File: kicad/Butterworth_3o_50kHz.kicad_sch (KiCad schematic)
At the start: 31 parts, among them J1 Conn_01x02_Pin, J2 Conn_01x02_Pin, J3 Conn_01x03_Pin, J4 Conn_01x02_Pin, J5 Conn_01x02_Pin, J6 Conn_01x02_Pin, J7 Conn_01x02_Pin, J8 Barrel_Jack, SW1 SW_DPDT_x2, SW2 SW_SPST, U1 TL072, U2 LM317L_TO92, U3 LMC7660

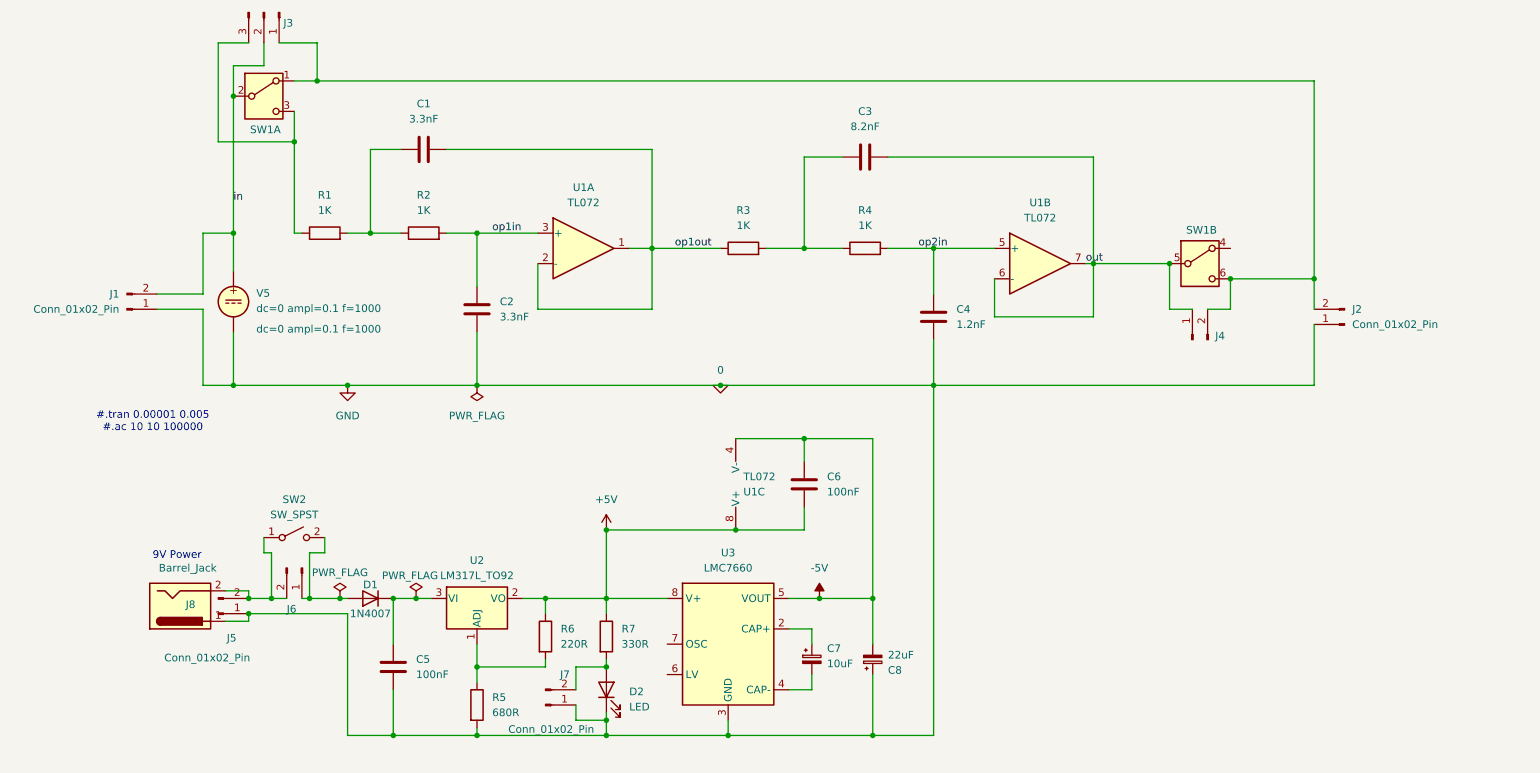
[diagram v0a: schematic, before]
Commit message: Corrected filenames to 50kHz instead of 40kHz
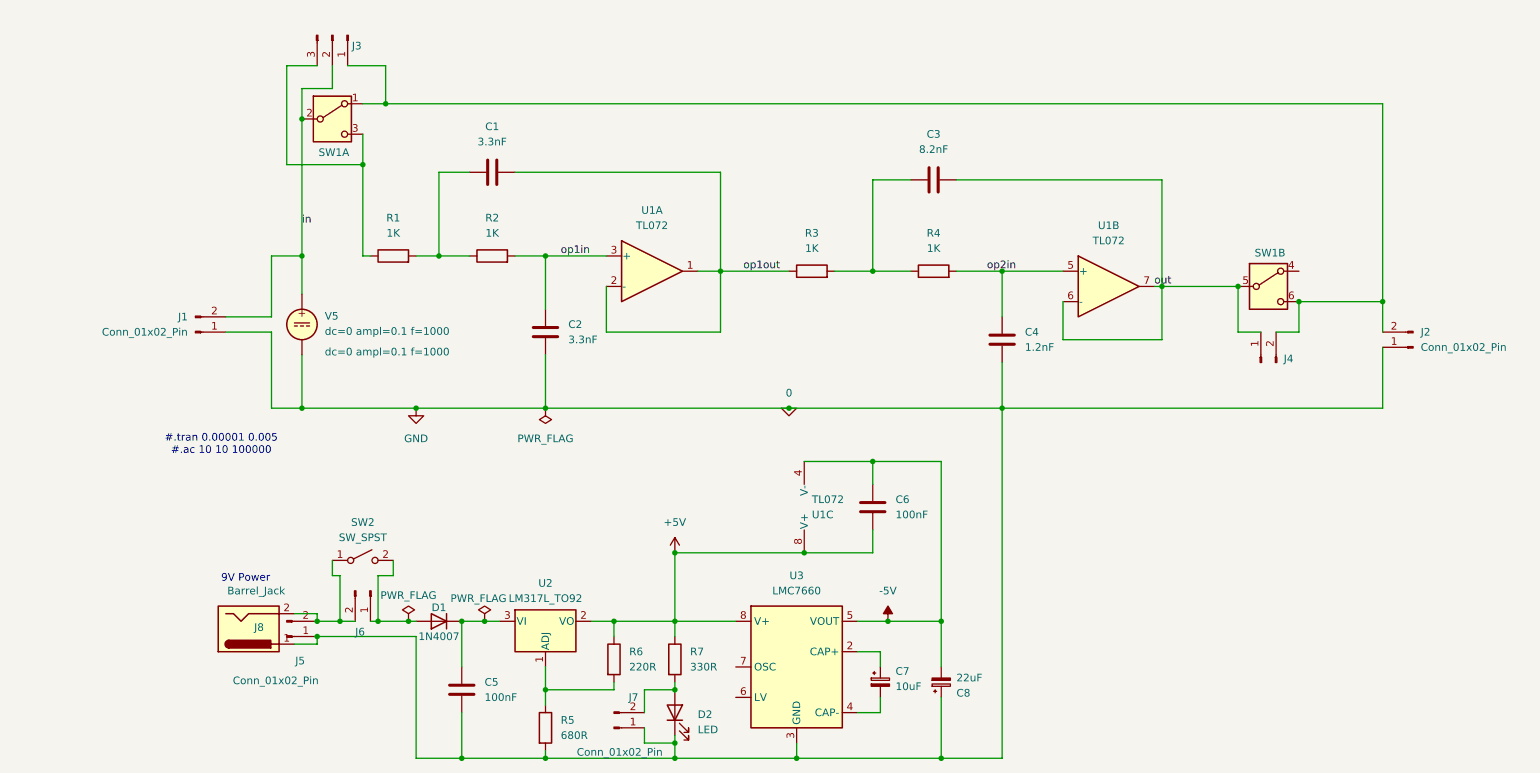
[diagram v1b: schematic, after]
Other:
- company: (none) -> acramonics
- title: (none) -> ScopeFilter (Butterworth 2rd Order LP filter 50kHz)
- moved on the sheet: C1, C2, C3, C4, C5, C6, C7, C8, D1, D2, J1, J2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
